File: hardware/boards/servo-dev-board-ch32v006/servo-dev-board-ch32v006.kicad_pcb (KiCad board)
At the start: 4 copper layers, 50 x 50 mm, 87 parts, among them J1 BATT JST-PH, J2 BUS JST-ZH, J3 BUS JST-ZH, J4 SERVO JST-ZH, J5 ENC JST-ZH, J6 DBG JST-ZH, Q1 AO3401A, Q2 AO3401A, Q3 AO3401A, SW1 SW_Push, U1 TPAP2210K-3.3TRG1, U2 74LVC2G125RA3-7, U3 DRV8837DSGR-JSM, U4 CH32V006F8U6

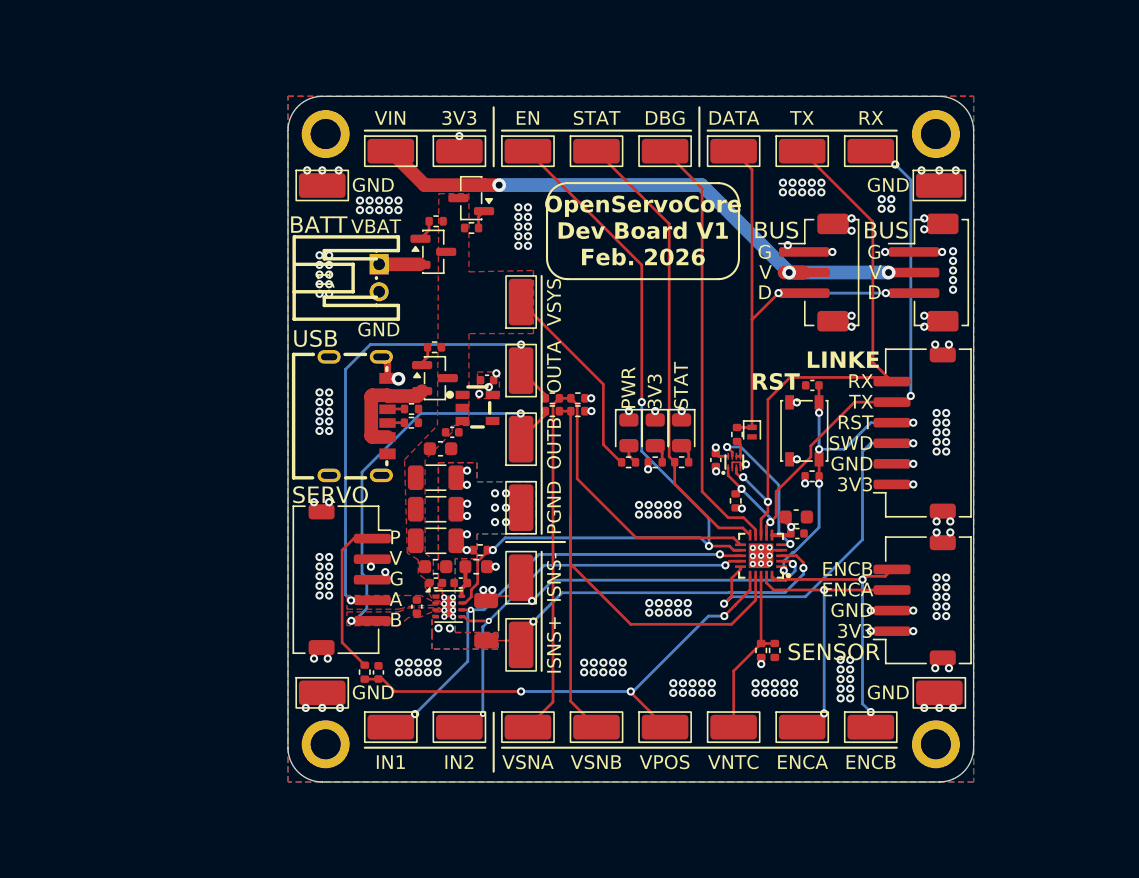
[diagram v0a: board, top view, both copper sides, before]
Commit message: Remove excessive ground via arrays
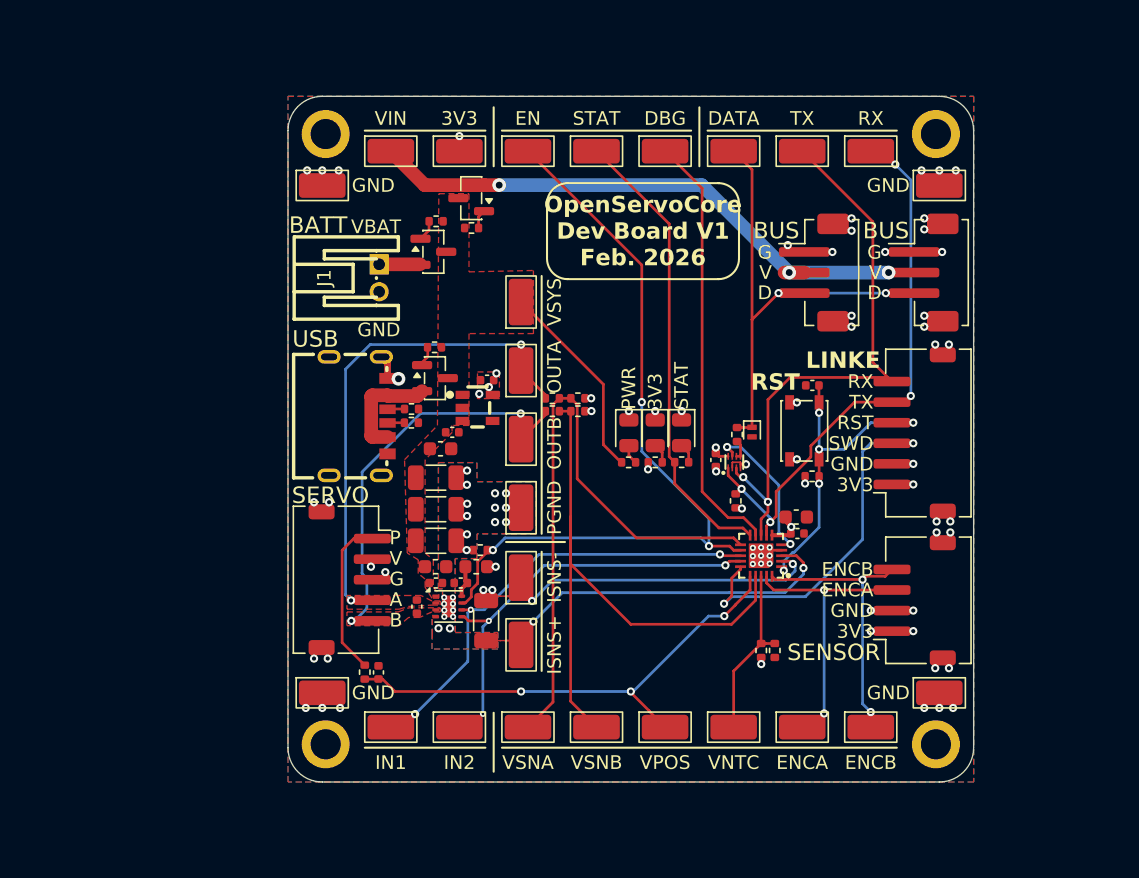
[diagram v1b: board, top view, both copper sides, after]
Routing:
- net GND: vias 220 -> 61

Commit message: routing ADC nets with higher priority so that measurements stay clean
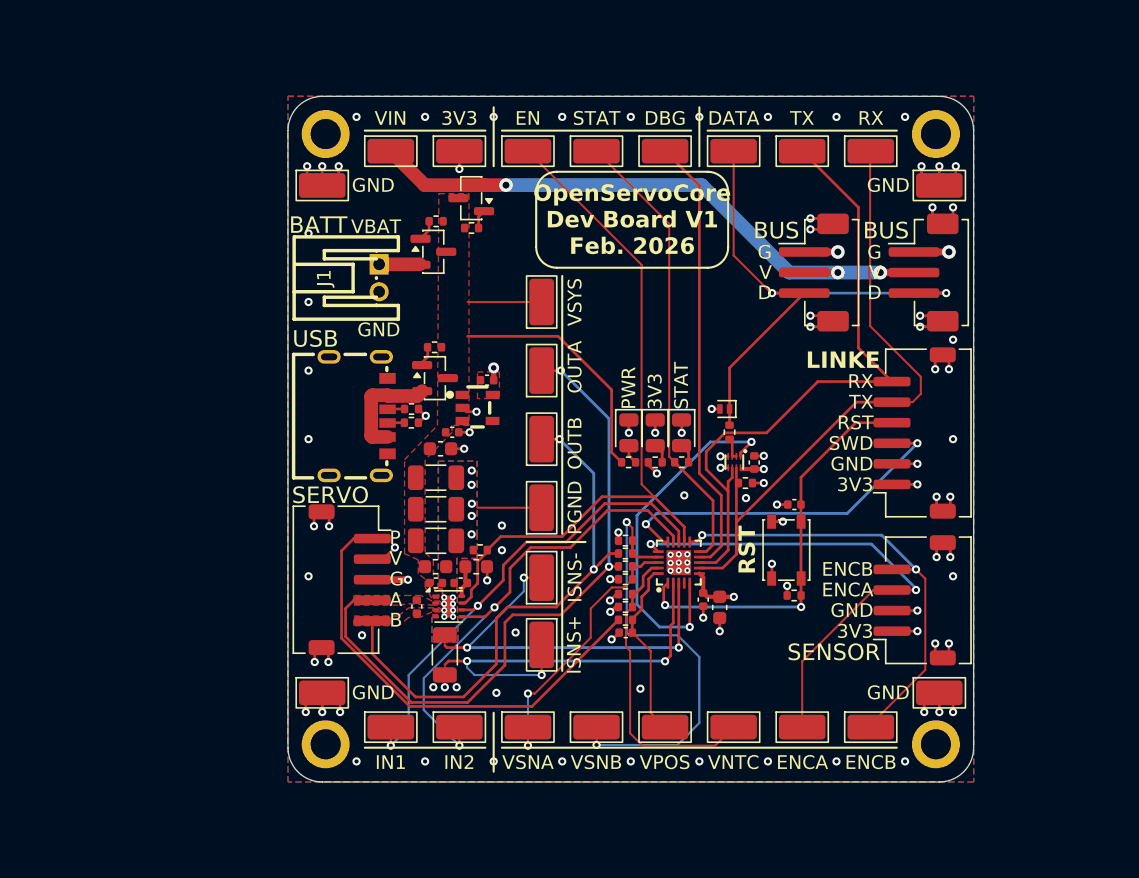
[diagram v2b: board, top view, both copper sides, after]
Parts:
- moved R6 19.4 mm to (154.6, 98.2), turned to 180 degrees
- moved C5 18.3 mm to (154.6, 99.1), turned to 180 degrees
- moved R16 13.6 mm to (154.6, 95.2), turned to 180 degrees
- moved R15 13.4 mm to (154.6, 94.3)
- moved R17 11.7 mm to (154.6, 93.3)
- moved TH1 11.3 mm to (154.6, 97.2), turned to 180 degrees
- moved R14 10.7 mm to (154.6, 96.3), turned to 0 degrees
- moved R18 10.1 mm to (154.6, 92.4), turned to 180 degrees
- moved R8 8.79 mm to (166.9, 96.4)
- moved C13 8.79 mm to (166.9, 89.8)
- moved SW1 8.79 mm to (166.3, 93.1)
- moved C14 8.64 mm to (161.5, 97.3), turned to -90 degrees
- moved C15 8.39 mm to (160.3, 96.7), turned to -90 degrees
- moved NT2 6.44 mm to (141.4, 101.5), turned to -90 degrees
- moved U4 6.02 mm to (158.5, 94.0), turned to 0 degrees
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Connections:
- R5 pad 1: /BUF -> /DATA
- R5 pad 2: /DATA -> /BUF
- TP25 pad 1: /ISNS- -> /ISNS+
- TP26 pad 1: /ISNS+ -> /ISNS-
- U2 pad 1: /TX -> /DE
- U2 pad 2: GND -> /BUF
- U2 pad 3: /RX -> /BUF
- U2 pad 5: /BUF -> GND
- U2 pad 6: /BUF -> /RX
- U2 pad 7: /DE -> /TX
- U4 pad 11: /VSNA -> /ENCB
- U4 pad 16: /VPOS -> /ENCA
- U4 pad 18: /VNTC -> /VSNA
- U4 pad 19: /ENCA -> /VNTC
- U4 pad 20: /ENCB -> /VPOS
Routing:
- net GND: track 5.21 -> 37.8 mm, vias 61 -> 103
- net /VSNA: track 45.7 -> 20.4 mm, vias 0 -> 2
- net /VPOS: track 36.2 -> 13.1 mm, vias 3 -> 0
- net /POT: track 11.6 -> 33.9 mm
- net /ENCA: track 18.8 -> 36.8 mm
- net /OUTA: track 33.3 -> 49.2 mm
- net /DE: track 10.4 -> 26.2 mm
- net /ENCB: track 19.1 -> 32.8 mm
- net /VSNB: track 45.9 -> 32.8 mm, vias 0 -> 2
- net /OUTB: track 27.8 -> 39.8 mm
- net +3.3V: track 3.80 -> 13.9 mm, vias 15 -> 12
- net /VNTC: track 12.8 -> 22.0 mm
- net /DATA: track 32.3 -> 40.8 mm
- net /nRST: track 21.0 -> 29.5 mm, vias 5 -> 2
- net VSYS: track 14.7 -> 23.1 mm
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
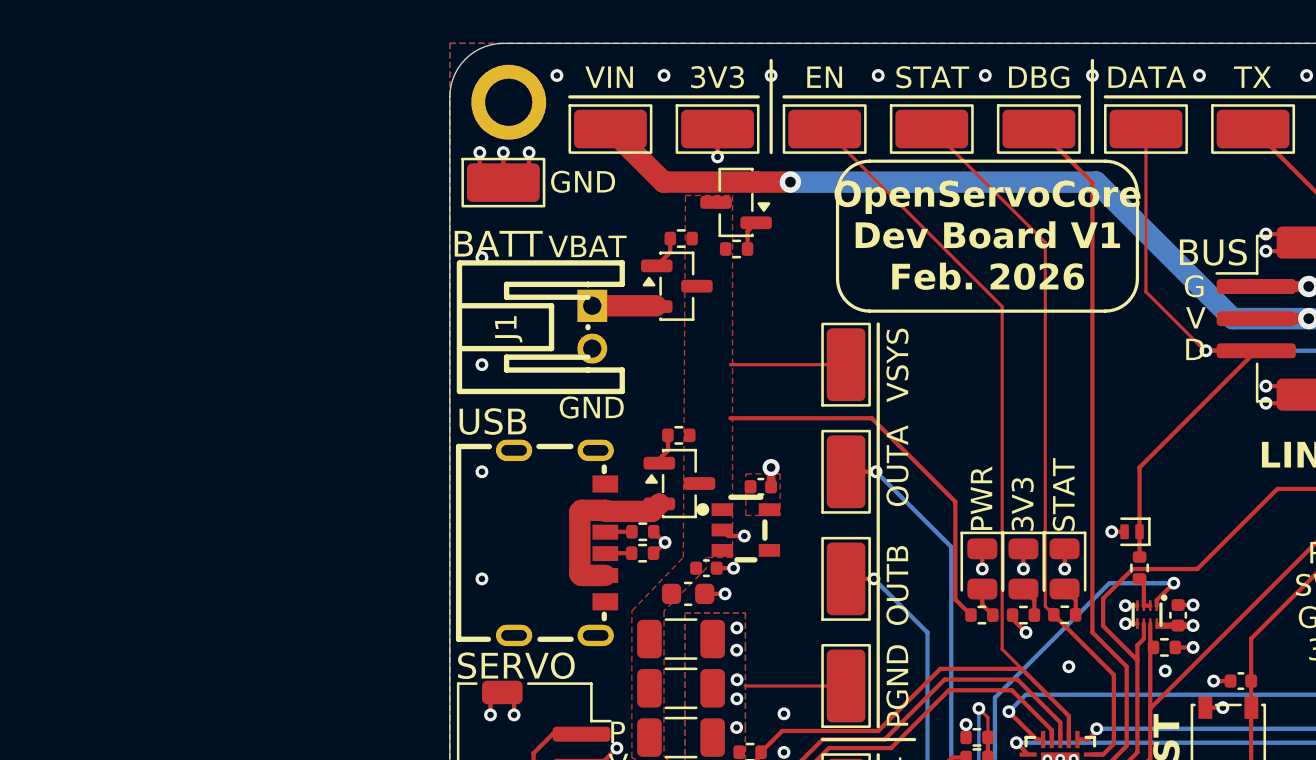
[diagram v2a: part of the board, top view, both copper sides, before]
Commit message: split schematics into sub sheets
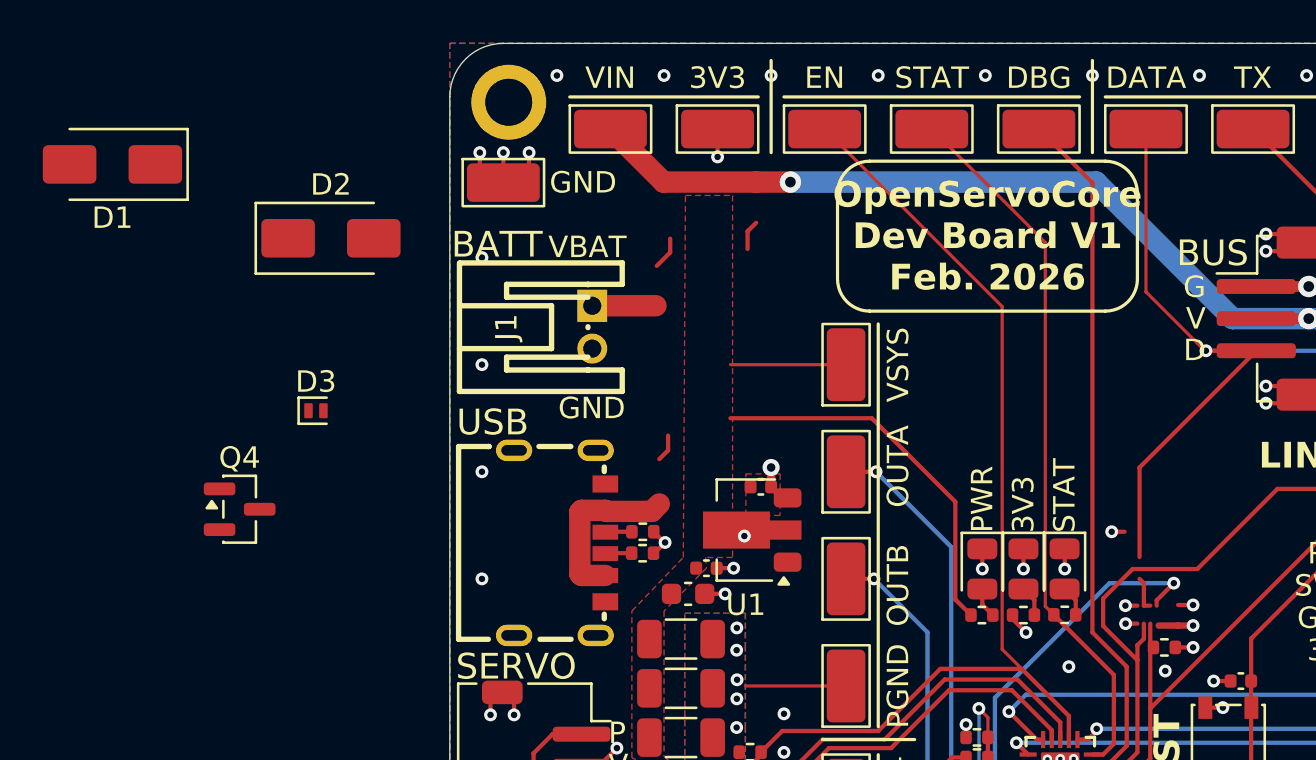
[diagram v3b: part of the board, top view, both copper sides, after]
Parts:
- removed C4: 0.1µF, Capacitor_SMD:C_0402_1005Metric
- removed Q1, Q2, Q3: AO3401A, Package_TO_SOT_SMD:SOT-23
- removed R1, R2, R3: 100kΩ, Resistor_SMD:R_0402_1005Metric
- removed R5: 49.9Ω, Resistor_SMD:R_0402_1005Metric
- removed U2: 74LVC2G125RA3-7, shared:X2-DFN1210-8_L1.2-W1.0-P0.30-BL
- added D2: SS34, Diode_SMD:D_SMA, F.Cu at (124.5, 69.1)
- added D3: ESD, Diode_SMD:D_SOD-882, F.Cu at (123.8, 77.2)
- added Q4: AO3400A, Package_TO_SOT_SMD:SOT-23, F.Cu at (120.2, 81.8)
- D1: value ESD -> SS34; footprint Diode_SMD:D_SOD-882 -> Diode_SMD:D_SMA
- R4: value 47kΩ -> 49.9Ω
- U1: value TPAP2210K-3.3TRG1 -> HT75xx-1-SOT89; footprint shared:SOT-23-5_L2.9-W1.6-P0.95-LS2.8-BR -> Package_TO_SOT_SMD:SOT-89-3
- moved D1 50.6 mm to (114.2, 65.7)
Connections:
- D1 pad 1: /DATA -> VSYS
- D1 pad 2: GND -> VBUS
- J2 pad 2: BUS_VIN -> VSYS
- J3 pad 2: BUS_VIN -> VSYS
- R4 pad 1: /TX -> Net-(Q4-S)
- R4 pad 2: +3.3V -> /UART
- TP12 pad 1: BUS_VIN -> VBAT
- TP15 pad 1: /STAT -> /DBG
- TP16 pad 1: /DBG -> /STAT
- TP17 pad 1: /DATA -> /RX
- TP18 pad 1: /RX -> /TX
- TP19 pad 1: /TX -> /DATA
- U1 pad 1: VSYS -> GND
- U1 pad 2: GND -> VSYS
- U1 pad 3: VSYS -> +3.3V
- U4 pad 10: /STAT -> /DBG
- U4 pad 5: /DE -> /UART
- U4 pad 9: /DBG -> /STAT
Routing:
- net (no net): track 0.00 -> 46.6 mm
- net BUS_VIN: track 40.8 -> 0.00 mm, vias 3 -> 0
- net /STAT: track 33.4 -> 65.9 mm
- net /DBG: track 32.4 -> 0.00 mm
- net /UART: track 0.00 -> 27.0 mm, vias 0 -> 2
- net /DE: track 26.2 -> 0.00 mm, vias 2 -> 0
- net /BUF: track 1.63 -> 0.00 mm
- net Net-(Q2-G): track 1.53 -> 0.00 mm
- net Net-(Q3-G): track 1.39 -> 0.00 mm
- net Net-(Q1-G): track 1.27 -> 0.00 mm
- net VSYS: track 23.1 -> 24.3 mm
- net GND: track 37.8 -> 36.7 mm
- net +3.3V: track 13.9 -> 13.1 mm
- net VBAT: vias 0 -> 3

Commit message: completed rework
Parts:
- removed C8: 0.1µF, Capacitor_SMD:C_0402_1005Metric
- removed C9: 10µF, Capacitor_SMD:C_0603_1608Metric
- removed Q4: AO3400A, Package_TO_SOT_SMD:SOT-23
- removed R17: 20kΩ, Resistor_SMD:R_0402_1005Metric
- removed R18: 10kΩ, Resistor_SMD:R_0402_1005Metric
- added C4: 0.1µF, Capacitor_SMD:C_0805_2012Metric_Pad1.18x1.45mm_HandSolder, F.Cu at (152.0, 90.3)
- added D4: PESD5V0L1BA, Diode_SMD:D_SOD-323_HandSoldering, F.Cu at (174.9, 71.7)
- added J7: PIN-V, Connector_PinHeader_2.54mm:PinHeader_1x03_P2.54mm_Vertical, F.Cu at (179.0, 63.5)
- added J8: PIN-V, Connector_PinHeader_2.54mm:PinHeader_1x03_P2.54mm_Vertical, F.Cu at (182.8, 63.5)
- added J9: JST-PH-V, shared:CONN-TH_B3B-PH-K-S, F.Cu at (188.0, 66.0)
- added R1: 5.1kΩ, Resistor_SMD:R_0805_2012Metric_Pad1.20x1.40mm_HandSolder, F.Cu at (141.7, 101.2)
- added R2: 5.1kΩ, Resistor_SMD:R_0805_2012Metric_Pad1.20x1.40mm_HandSolder, F.Cu at (141.7, 99.2)
- added R3: 1.5kΩ, Resistor_SMD:R_0805_2012Metric_Pad1.20x1.40mm_HandSolder, F.Cu at (171.2, 62.9)
- added R5: 20kΩ, Resistor_SMD:R_0805_2012Metric_Pad1.20x1.40mm_HandSolder, F.Cu at (154.0, 76.9)
- added TP27: TestPoint_Probe, TestPoint:TestPoint_Keystone_5015_Micro_Mini, F.Cu at (158.0, 68.0)
- added TP28: TestPoint_Probe, TestPoint:TestPoint_Keystone_5015_Micro_Mini, F.Cu at (158.0, 103.0)
- added U2: DRV8212PDSGR, Package_SON:WSON-8-1EP_2x2mm_P0.5mm_EP0.9x1.6mm, F.Cu at (149.3, 92.6)
- C1: footprint Capacitor_SMD:C_0603_1608Metric -> Capacitor_SMD:C_0805_2012Metric_Pad1.18x1.45mm_HandSolder
- C10, C12: value 47µF -> 0.1µF; footprint Capacitor_SMD:C_1206_3216Metric -> Capacitor_SMD:C_0805_2012Metric_Pad1.18x1.45mm_HandSolder
- C11: value 47µF -> 10µF; footprint Capacitor_SMD:C_1206_3216Metric -> Capacitor_SMD:C_0805_2012Metric_Pad1.18x1.45mm_HandSolder
- C13, C15, C2, C3, C5: footprint Capacitor_SMD:C_0402_1005Metric -> Capacitor_SMD:C_0805_2012Metric_Pad1.18x1.45mm_HandSolder
- C14: value 10µF -> 0.1µF; footprint Capacitor_SMD:C_0603_1608Metric -> Capacitor_SMD:C_0805_2012Metric_Pad1.18x1.45mm_HandSolder
- C6: value 0.1µF -> 10µF; footprint Capacitor_SMD:C_0402_1005Metric -> Capacitor_SMD:C_0805_2012Metric_Pad1.18x1.45mm_HandSolder
- C7: value 0.1µF -> 100µF; footprint Capacitor_SMD:C_0402_1005Metric -> Capacitor_SMD:CP_Elec_6.3x5.4
- D1, D2: value SS34 -> SS54; footprint Diode_SMD:D_SMA -> Diode_SMD:D_SMA_Handsoldering
- D3: value ESD -> SS54; footprint Diode_SMD:D_SOD-882 -> Diode_SMD:D_SMA_Handsoldering
- FB1: footprint Inductor_SMD:L_0603_1608Metric -> Inductor_SMD:L_0805_2012Metric_Pad1.05x1.20mm_HandSolder
- J1: value BATT JST-PH -> JST-PH-H
- J2: value BUS JST-ZH -> TERM; footprint Connector_JST:JST_ZH_B3B-ZR-SM4-TF_1x03-1MP_P1.50mm_Vertical -> shared:CONN-TH_2P-P5.00_WJ500V-5.08-2P
- J3: value BUS JST-ZH -> PIN-V; footprint Connector_JST:JST_ZH_B3B-ZR-SM4-TF_1x03-1MP_P1.50mm_Vertical -> Connector_PinHeader_2.54mm:PinHeader_2x03_P2.54mm_Vertical
- J4: value SERVO JST-ZH -> JST-ZH-H; footprint Connector_JST:JST_ZH_S5B-ZR-SM4A-TF_1x05-1MP_P1.50mm_Horizontal -> shared:CONN-TH_S5B-ZR-LF-SN
- J5: value ENC JST-ZH -> PIN-V; footprint Connector_JST:JST_ZH_S4B-ZR-SM4A-TF_1x04-1MP_P1.50mm_Horizontal -> Connector_PinHeader_2.54mm:PinHeader_1x05_P2.54mm_Vertical
- J6: value DBG JST-ZH -> PIN-V; footprint Connector_JST:JST_ZH_S6B-ZR-SM4A-TF_1x06-1MP_P1.50mm_Horizontal -> Connector_PinHeader_2.54mm:PinHeader_2x02_P2.54mm_Vertical
- R10: value 5.1kΩ -> 1kΩ; footprint Resistor_SMD:R_0402_1005Metric -> Resistor_SMD:R_0805_2012Metric_Pad1.20x1.40mm_HandSolder
- R11: value 2.2kΩ -> 10kΩ; footprint Resistor_SMD:R_0402_1005Metric -> Resistor_SMD:R_0805_2012Metric_Pad1.20x1.40mm_HandSolder
- R12: value 330Ω -> 10kΩ; footprint Resistor_SMD:R_0402_1005Metric -> Resistor_SMD:R_0805_2012Metric_Pad1.20x1.40mm_HandSolder
- R13: value 1KΩ -> 4.7kΩ; footprint Resistor_SMD:R_0402_1005Metric -> Resistor_SMD:R_0805_2012Metric_Pad1.20x1.40mm_HandSolder
- R14, R16, R8: footprint Resistor_SMD:R_0402_1005Metric -> Resistor_SMD:R_0805_2012Metric_Pad1.20x1.40mm_HandSolder
- R15: value 20kΩ -> 10kΩ; footprint Resistor_SMD:R_0402_1005Metric -> Resistor_SMD:R_0805_2012Metric_Pad1.20x1.40mm_HandSolder
- R4: value 49.9Ω -> 470Ω; footprint Resistor_SMD:R_0402_1005Metric -> Resistor_SMD:R_0805_2012Metric_Pad1.20x1.40mm_HandSolder
- R6: value 4.7kΩ -> 10kΩ; footprint Resistor_SMD:R_0402_1005Metric -> Resistor_SMD:R_0805_2012Metric_Pad1.20x1.40mm_HandSolder
- R7: value 10kΩ -> 20kΩ; footprint Resistor_SMD:R_0402_1005Metric -> Resistor_SMD:R_0805_2012Metric_Pad1.20x1.40mm_HandSolder
- R9: value 5.1kΩ -> 10kΩ; footprint Resistor_SMD:R_0402_1005Metric -> Resistor_SMD:R_0805_2012Metric_Pad1.20x1.40mm_HandSolder
- RS1: value 0.1Ω 1% -> 100mΩ 1%
- SW1: footprint Button_Switch_SMD:SW_SPST_PTS810 -> Button_Switch_SMD:SW_SPST_TS-1088-xR020
- TH1: value NTC 10k -> 10kΩ 3950K; footprint Resistor_SMD:R_0402_1005Metric -> Resistor_SMD:R_0805_2012Metric_Pad1.20x1.40mm_HandSolder
- U1: value HT75xx-1-SOT89 -> HT7533-1; footprint Package_TO_SOT_SMD:SOT-89-3 -> Package_TO_SOT_SMD:SOT-89-3_Handsoldering
- U3: value DRV8837DSGR-JSM -> CH32V006F8P6; footprint Package_SON:WSON-8-1EP_2x2mm_P0.5mm_EP0.9x1.6mm -> Package_SO:TSSOP-20_4.4x6.5mm_P0.65mm
- U4: value CH32V006F8U6 -> 74LVC2G241; footprint shared:UQFN-20_L3.0-W3.0-P0.40-BL-EP1.7 -> Package_SO:VSSOP-8_2.3x2mm_P0.5mm
- USB1: value TYPE-C 6P(073) -> TYPE-C-H
- moved D1 37.4 mm to (135.0, 96.8), turned to 0 degrees
- moved R10 36.2 mm to (171.2, 67.3)
- moved J5 35.7 mm to (142.5, 83.7), turned to 0 degrees
- moved TH1 33.1 mm to (184.0, 82.1), turned to 0 degrees
- moved J2 31.6 mm to (137.4, 66.3), turned to 90 degrees
- moved SW1 30.1 mm to (153.0, 66.1), turned to 0 degrees
- moved C12 29.8 mm to (166.8, 102.5)
- moved C13 29.6 mm to (147.8, 67.2)
- moved R15 29.3 mm to (180.2, 80.1)
- moved R8 28.6 mm to (154.0, 70.9), turned to 180 degrees
- moved R12 28.0 mm to (184.0, 80.1), turned to 180 degrees
- moved C11 27.9 mm to (166.8, 100.2)
- moved U3 27.3 mm to (169.0, 95.3)
- moved C3 26.4 mm to (153.8, 105.5), turned to -90 degrees
- moved R7 26.2 mm to (154.0, 68.9), turned to 0 degrees
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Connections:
- C10 pad 1: VSYS -> /MOT_A
- C10 pad 2: PGND -> /MOT_B
- C11 pad 1: VSYS -> +3V3
- C11 pad 2: PGND -> GND
- C12 pad 1: VSYS -> +3V3
- C12 pad 2: PGND -> GND
- C13 pad 2: /nRST -> /MCU/nRST
- C14 pad 1: +3.3V -> /VPOS
- C15 pad 1: +3.3V -> +3V3
- C3 pad 1: +3.3V -> +3V3
- C5 pad 1: /VPOS -> VSYS
- C5 pad 2: GND -> PGND
- C6 pad 1: /3V3_DRV -> VSYS
- C7 pad 1: /OUTA -> VSYS
- C7 pad 2: /OUTB -> PGND
- D3 pad 1: /DATA -> VSYS
- D3 pad 2: GND -> VEXT
- FB1 pad 1: +3.3V -> +3V3
- FB1 pad 2: /3V3_DRV -> /M_DRV/+3V3_DRV
- J2 pad 1: GND -> VEXT
- J2 pad 2: VSYS -> GND
- J3 pad 1: GND -> +3V3
- J3 pad 2: VSYS -> GND
- J3 pad 3: /DATA -> /MCU/SWDIO
- J4 pad 1: /POT -> GND
- J4 pad 2: +3.3V -> /SERVO_IO/POT
- J4 pad 3: GND -> +3V3
- J4 pad 4: /OUTA -> /MOT_A
- J4 pad 5: /OUTB -> /MOT_B
- J5 pad 1: +3.3V -> GND
- J5 pad 2: GND -> /SERVO_IO/POT
- J5 pad 3: /ENCA -> +3V3
- J5 pad 4: /ENCB -> /MOT_A
- J6 pad 1: +3.3V -> +3V3
- J6 pad 3: /SWDIO -> /ENCA
- J6 pad 4: /nRST -> /ENCB
- LED1 pad 2: Net-(LED1-A) -> /POWER/LED_VSYS
- LED2 pad 2: Net-(LED2-A) -> /POWER/LED_3V3
- R10 pad 1: GND -> /STAT
- R10 pad 2: Net-(USB1-CC2) -> Net-(LED3-A)
- R11 pad 1: VSYS -> +3V3
- R11 pad 2: Net-(LED1-A) -> /MCU/nRST
- R12 pad 1: +3.3V -> +3V3
- R12 pad 2: Net-(LED2-A) -> /VNTC
- R13 pad 1: /STAT -> /VPOS
- R13 pad 2: Net-(LED3-A) -> /SERVO_IO/POT
- R14 pad 1: +3.3V -> +3V3
- R14 pad 2: /VNTC -> /RX
- R15 pad 1: /OUTA -> /TX_EN
- R15 pad 2: /VSNA -> GND
- R16 pad 1: /VSNA -> +3V3
- R16 pad 2: GND -> /DATA
- R4 pad 1: Net-(Q4-S) -> +3V3
- R4 pad 2: /UART -> /POWER/LED_3V3
- R6 pad 1: /VPOS -> /VSNA
- R6 pad 2: /POT -> GND
- R7 pad 1: /EN -> /MOT_B
- R7 pad 2: PGND -> /VSNB
- R8 pad 1: +3.3V -> /VSNB
- R8 pad 2: /nRST -> GND
- R9 pad 1: GND -> /EN
- R9 pad 2: Net-(USB1-CC1) -> PGND
- SW1 pad 1: /nRST -> /MCU/nRST
- TP12 pad 1: VBAT -> +3V3
- TP13 pad 1: +3.3V -> /EN
- TP14 pad 1: /EN -> /DBG
- TP15 pad 1: /DBG -> /STAT
- TP16 pad 1: /STAT -> /RX
- TP17 pad 1: /RX -> /TX
- TP18 pad 1: /TX -> /TX_EN
- TP22 pad 1: /OUTA -> /MOT_A
- TP23 pad 1: /OUTB -> /MOT_B
- TP25 pad 1: /ISNS+ -> /ISNS-
- TP26 pad 1: /ISNS- -> /ISNS+
- U1 pad 3: +3.3V -> +3V3
- U3 pad 1: VSYS -> /VPOS
- U3 pad 2: /OUTA -> /VSNA
- U3 pad 3: /OUTB -> /VSNB
- U3 pad 4: PGND -> /MCU/nRST
- U3 pad 5: /IN2 -> /ISNS-
- U3 pad 6: /IN1 -> /ISNS+
- U3 pad 7: /EN -> +3V3
- U3 pad 8: /3V3_DRV -> /STAT
- U3 pad 9: PGND -> GND
- U4 pad 1: /nRST -> /TX_EN
- U4 pad 2: /ISNS- -> /DATA
- U4 pad 3: /ISNS+ -> /DATA
- U4 pad 5: /UART -> /TX
- U4 pad 6: +3.3V -> /RX
- U4 pad 7: /TX -> /TX_EN
- U4 pad 8: /RX -> +3V3
- USB1 pad A5: Net-(USB1-CC1) -> /POWER/CC2
- USB1 pad B5: Net-(USB1-CC2) -> /POWER/CC1
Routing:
- net /MCU/nRST: track 0.00 -> 71.5 mm, vias 0 -> 2
- net /MOT_B: track 0.00 -> 56.2 mm, vias 0 -> 2
- net /TX_EN: track 0.00 -> 53.1 mm, vias 0 -> 2
- net /DBG: track 0.00 -> 50.8 mm, vias 0 -> 2
- net /VPOS: track 13.1 -> 63.6 mm, vias 0 -> 2
- net /OUTA: track 49.2 -> 0.00 mm, vias 2 -> 0
- net (no net): track 46.6 -> 0.00 mm
- net /VNTC: track 22.0 -> 65.5 mm, vias 0 -> 2
- net /VSNB: track 32.8 -> 74.6 mm
- net /OUTB: track 39.8 -> 0.00 mm, vias 2 -> 0
- net /SERVO_IO/POT: track 0.00 -> 35.2 mm
- net /VSNA: track 20.4 -> 55.3 mm
- net /MOT_A: track 0.00 -> 34.6 mm
- net /POT: track 33.9 -> 0.00 mm
- net GND: track 36.7 -> 3.45 mm, vias 103 -> 69
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- added copper zone on In2.Cu, net +3V3
- added copper zone on F.Cu, net /MOT_A
- added copper zone on F.Cu, net /MOT_B
- added copper zone on F.Cu, net VBAT
- added copper zone on F.Cu, net VBUS
- added copper zone on F.Cu, net VEXT
- added copper zone on B.Cu, net VSYS
- removed copper zone on F.Cu, net +3.3V
- removed copper zone on In2.Cu, net +3.3V
- removed copper zone on F.Cu, net /OUTA
- removed copper zone on F.Cu, net /OUTB
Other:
- board size 50 x 50 mm -> 60 x 60 mm
- board text added: "+"
- board text added: "-"
- board text added: "BRD: servo-dev-board-ch32v006 MCU: CH32V006F8P6 DRV: DRV8212PDSGR LDO: HT7533-1 BUF: 74LVC2G241 RS1: 0.1Ohm ~1% 250mW REV: A"
- board text added: "D3"
- board text added: "DXL TTL"
- board text added: "Encoder"
- board text added: "G V D"
- board text added: "HDR 2X2P"
- board text added: "HDR 2X3P"
- board text added: "HDR-3P"
- board text added: "ISN+"
- board text added: "ISN-"
- board text added: "JST-PH 2P"
- board text added: "JST-PH-3P"
- board text added: "JST-ZH 5P"
- board text added: "LinkE"
- board text added: "M2 Ø2.2"
- board text added: "RESET"
- board text added: "S"
- board text added: "SRVINT"
- board text added: "SYS"
- board text added: "TERM-5.08 2P"
- board text added: "USB-C PWR"
- board text added: "VBUS"
- board text removed: "BATT"
- board text removed: "BRD: servo-dev-board-ch32v006 MCU: CH32V006F8U6 DRV: DRV8837DSGR-JSM LDO: TPAP2210K-3.3TRG1 BUF: 74LVC2G125RA3-7 RS1: 0.1 OHM ~1%"
- board text removed: "BUS"
- board text removed: "D"
- board text removed: "ISNS+"
- board text removed: "ISNS-"
- board text removed: "JST-PH-2P"
- board text removed: "JST-ZH-3P"
- board text removed: "JST-ZH-4P"
- board text removed: "JST-ZH-5P"
- board text removed: "JST-ZH-6P"
- board text removed: "LINKE"
- board text removed: "P"
- board text removed: "R12"
- board text removed: "SENSOR"
- board text removed: "SERVO"
- board text removed: "USB"
